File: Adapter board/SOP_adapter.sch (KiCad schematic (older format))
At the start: 5 parts, among them J1 Conn_01x03_Female, J2 Conn_01x24_Female, J3 Conn_01x24_Female, U1 AMS1117-3.3, U2 STM32F103C8Tx

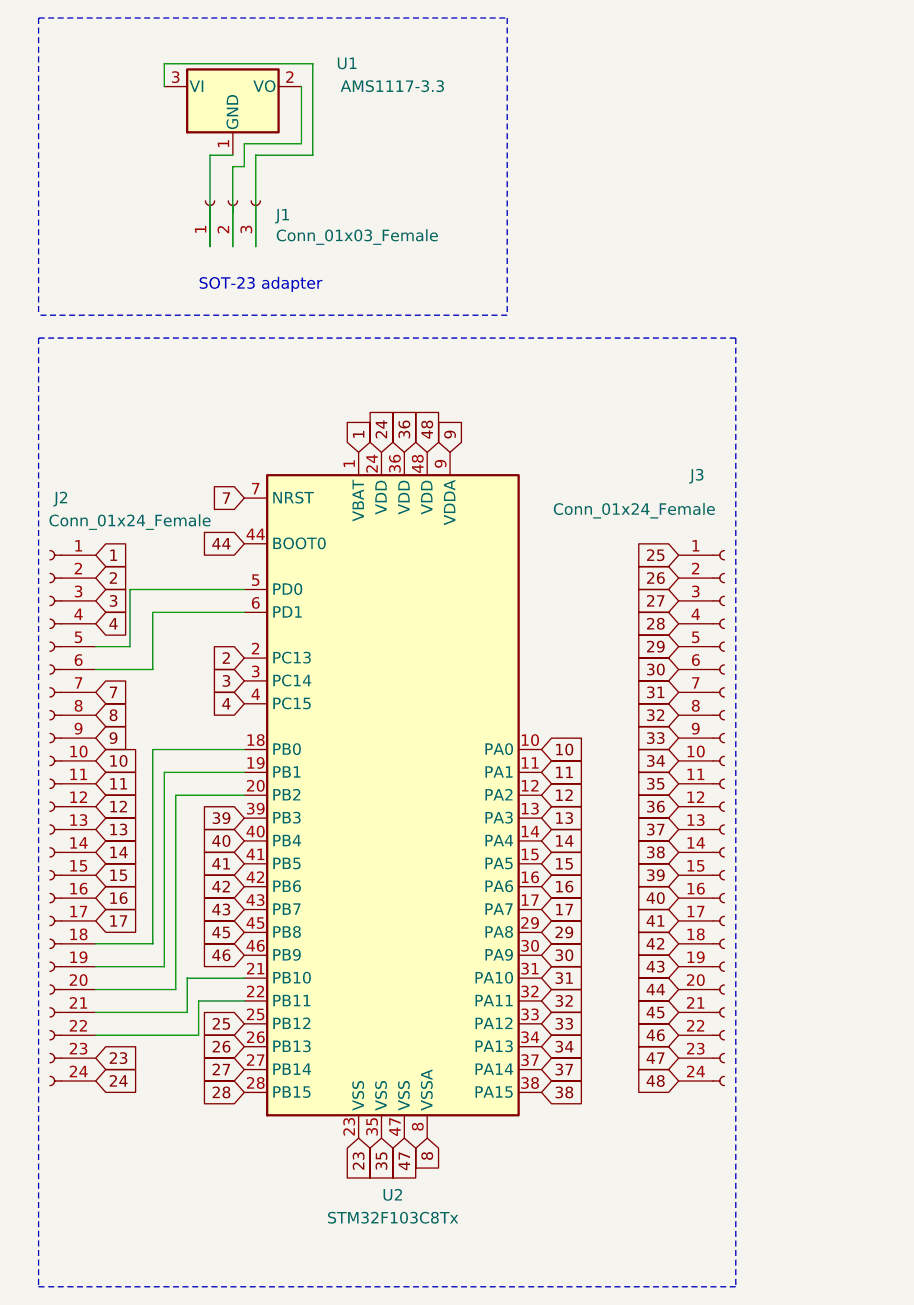
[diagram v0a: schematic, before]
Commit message: Add files via upload
updated qfnp48 header pins to 02x06
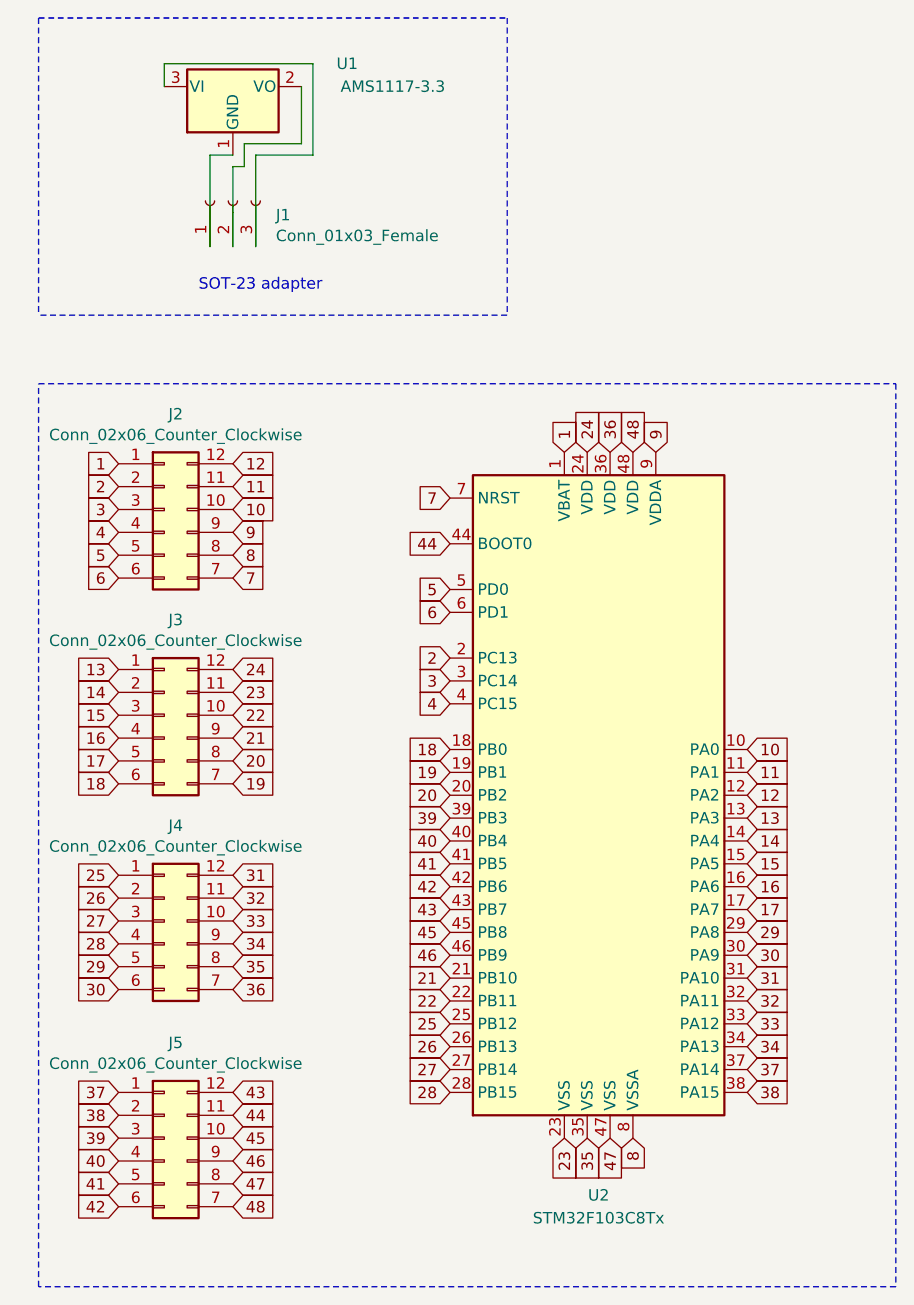
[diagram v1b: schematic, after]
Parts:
- removed J2, J3: Conn_01x24_Female, Connector_PinHeader_2.54mm:PinHeader_1x24_P2.54mm_Vertical, symbol Connector:Conn_01x24_Female
- added J2, J3, J4, J5: Conn_02x06_Counter_Clockwise, Connector_PinHeader_2.54mm:PinHeader_2x06_P2.54mm_Vertical, symbol Connector_Generic:Conn_02x06_Counter_Clockwise
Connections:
- net 1: now also J2.1 (Pin_1)
- net 10: now also J2.10 (Pin_10)
- net 11: now also J2.11 (Pin_11)
- net 12: now also J2.12 (Pin_12)
- net 13: now also J3.1 (Pin_1)
- net 14: now also J3.2 (Pin_2)
- net 15: now also J3.3 (Pin_3)
- net 16: now also J3.4 (Pin_4)
- net 17: now also J3.5 (Pin_5)
- net 2: now also J2.2 (Pin_2)
- net 23: now also J3.11 (Pin_11)
- net 24: now also J3.12 (Pin_12)
- net 25: now also J4.1 (Pin_1)
- net 26: now also J4.2 (Pin_2)
- net 27: now also J4.3 (Pin_3)
- net 28: now also J4.4 (Pin_4)
- net 29: now also J4.5 (Pin_5)
- net 3: now also J2.3 (Pin_3)
- net 30: now also J4.6 (Pin_6)
- net 31: now also J4.12 (Pin_12)
- net 32: now also J4.11 (Pin_11)
- net 33: now also J4.10 (Pin_10)
- net 34: now also J4.9 (Pin_9)
- net 35: now also J4.8 (Pin_8)
- net 36: now also J4.7 (Pin_7)
- net 37: now also J5.1 (Pin_1)
- net 38: now also J5.2 (Pin_2)
- net 39: now also J5.3 (Pin_3)
- net 4: now also J2.4 (Pin_4)
- net 40: now also J5.4 (Pin_4)
- net 41: now also J5.5 (Pin_5)
- net 42: now also J5.6 (Pin_6)
- net 43: now also J5.12 (Pin_12)
- net 44: now also J5.11 (Pin_11)
- net 45: now also J5.10 (Pin_10)
- net 46: now also J5.9 (Pin_9)
- net 47: now also J5.8 (Pin_8)
- net 48: now also J5.7 (Pin_7)
- net 7: now also J2.7 (Pin_7)
- net 8: now also J2.8 (Pin_8)
- net 9: now also J2.9 (Pin_9)
- net 18: now reaches U2.18 (PB0)
- net 18: now also J3.6 (Pin_6)
- net 19: now reaches U2.19 (PB1)
- net 19: now also J3.7 (Pin_7)
- net 20: now reaches U2.20 (PB2)
- net 20: now also J3.8 (Pin_8)
- net 21: now reaches U2.21 (PB10)
- net 21: now also J3.9 (Pin_9)
- net 22: now reaches U2.22 (PB11)
- net 22: now also J3.10 (Pin_10)
- net 5: now reaches U2.5 (PD0)
- net 5: now also J2.5 (Pin_5)
- net 6: now reaches U2.6 (PD1)
- net 6: now also J2.6 (Pin_6)
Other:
- moved on the sheet: U2
